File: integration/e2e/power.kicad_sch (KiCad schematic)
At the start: 2 parts

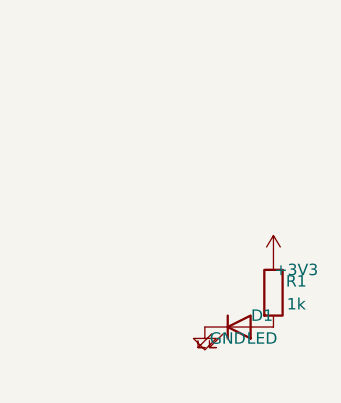
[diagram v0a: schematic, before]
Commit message: feat(e2e): lay out the e2e schematic with straight wires
The first e2e sheets connected parts pin to pin, on A4: correct (ERC
clean) but hard to read, with parts on top of each other in a corner.
Now:

* both sheets are A5, with title blocks (title, date, revision, a note);
* every wire is straight. On the root sheet, each pin of J1 runs left
  to its rail, +3V3 and its power flag above, GND and its flag below,
  with a junction on each rail. On "Power", +3V3, R1, D1 (turned so its
  anode is on top) and GND form one column;
* D1's reference and value read horizontally.

The nets, parts and UUIDs are unchanged, so the board still matches.
KiCad 9.0.9, on the design staged as kicad_pcb stages it: ERC 0
violations; DRC 0 violations, 0 unconnected, 0 parity issues; netlist
+3V3 (J1.1, R1.1), GND (D1.K, J1.2), Net-(D1-A) (D1.A, R1.2).

This commit has been created by an automated coding assistant,
with human supervision.

Prompt:
why do these sample e2e designs have doglegs in schematics, when all
wires could be mostly straight?

Co-Authored-By: Claude Opus 5.5 <noreply@anthropic.com>
Claude-Session: https://claude.ai/code/session_01WoWXzhMvNxH4iJRPTWT44f
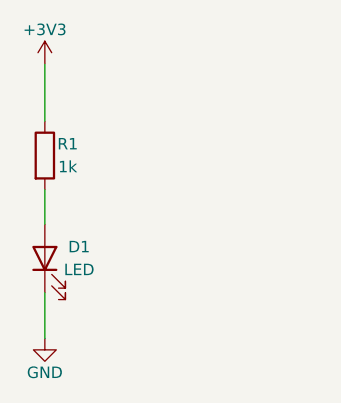
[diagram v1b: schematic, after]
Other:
- company: (none) -> rules_kicad
- title: (none) -> rules_kicad e2e design: Power
- moved on the sheet: D1, R1
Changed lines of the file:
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@@
 	(generator "eeschema")
 	(generator_version "9.0")
-	(paper "A4")
+	(paper "A5")
+	(title_block
+		(title "rules_kicad e2e design: Power")
+		(date "2026-10-29")
+		(rev "1")
+		(company "rules_kicad")
+		(comment 1 "R1 sets the LED current: (3.3 V - 2 V) / 1 kOhm = 1.3 mA")
+	)
+	(symbol
+		(lib_id "power:+3V3")
+		(at 76.2 50.8 0)
+		(unit 1)
+		(exclude_from_sim no)
+		(in_bom no)
+		(on_board no)
+		(dnp no)
+		(property "Reference" "#PWR03"
+			(at 76.2 44.45 0)
+			(effects
+				(font
+					(size 1.27 1.27)
+				)
+				(hide yes)
+			)
+		)
+		(property "Value" "+3V3"
+			(at 76.2 46.99 0)
+			(effects
+				(font
+					(size 1.27 1.27)
+				)
+			)
+		)
+		(property "Footprint" ""
+			(at 76.2 50.8 0)
+			(effects
+				(font
+					(size 1.27 1.27)
+				)
+				(hide yes)
+			)
+		)
+		(property "Datasheet" "~"
+			(at 76.2 50.8 0)
+			(effects
+				(font
+					(size 1.27 1.27)
+				)
+				(hide yes)
+			)
+		)
+		(property "Description" ""
+			(at 76.2 50.8 0)
+			(effects
+				(font
+					(size 1.27 1.27)
+				)
+				(hide yes)
+			)
+		)
+		(pin "1"
+		)
+		(instances
+			(project "main"
+				(path "/02c35194-34ab-516c-8342-afa9fed2f47f/4a82951d-9541-5098-92db-96b4b94b7393"
+					(reference "#PWR03")
+					(unit 1)
+				)
+			)
+		)
+	)
 	(symbol
 		(lib_id "Device:R")
-		(at 101.6 76.2 0)
+		(at 76.2 60.96 0)
 		(unit 1)
 		(exclude_from_sim no)
@@
 		(dnp no)
 		(property "Reference" "R1"
-			(at 104.14 74.93 0)
+			(at 78.74 59.69 0)
 			(effects
 				(font
@@
 		)
 		(property "Value" "1k"
-			(at 104.14 77.47 0)
+			(at 78.74 62.23 0)
 			(effects
 				(font
@@
 		)
 		(property "Footprint" "Resistor_SMD:R_0603_1608Metric"
-			(at 101.6 76.2 0)
-			(effects
-				(font
-					(size 1.27 1.27)
-				)
-				(hide yes)
-			)
-		)
-		(property "Datasheet" "~"
-			(at 101.6 76.2 0)
-			(effects
-				(font
-					(size 1.27 1.27)
-				)
-				(hide yes)
-			)
-		)
-		(property "Description" ""
-			(at 101.6 76.2 0)
+			(at 76.2 60.96 0)
+			(effects
+				(font
+					(size 1.27 1.27)
+				)
+				(hide yes)
+			)
+		)
+		(property "Datasheet" "~"
+			(at 76.2 60.96 0)
+			(effects
+				(font
+					(size 1.27 1.27)
+				)
+				(hide yes)
+			)
+		)
+		(property "Description" ""
+			(at 76.2 60.96 0)
 			(effects
 				(font
@@
 	(symbol
 		(lib_id "Device:LED")
-		(at 97.79 80.01 0)
+		(at 76.2 72.39 90)
 		(unit 1)
 		(exclude_from_sim no)
@@
 		(dnp no)
 		(property "Reference" "D1"
-			(at 100.33000000000001 78.74000000000001 0)
+			(at 80.01 71.12 90)
 			(effects
 				(font
@@
 		)
 		(property "Value" "LED"
-			(at 100.33000000000001 81.28 0)
+			(at 80.01 73.66 90)
 			(effects
 				(font
@@
 		)
 		(property "Footprint" "LED_SMD:LED_0603_1608Metric"
-			(at 97.79 80.01 0)
-			(effects
-				(font
-					(size 1.27 1.27)
-				)
-				(hide yes)
-			)
-		)
-		(property "Datasheet" "~"
-			(at 97.79 80.01 0)
-			(effects
-				(font
-					(size 1.27 1.27)
-				)
-				(hide yes)
-			)
-		)
-		(property "Description" ""
-			(at 97.79 80.01 0)
+			(at 76.2 72.39 0)
+			(effects
+				(font
+					(size 1.27 1.27)
+				)
+				(hide yes)
+			)
+		)
+		(property "Datasheet" "~"
+			(at 76.2 72.39 0)
+			(effects
+				(font
+					(size 1.27 1.27)
+				)
+				(hide yes)
+			)
+		)
+		(property "Description" ""
+			(at 76.2 72.39 0)
 			(effects
 				(font
@@
 	)
 	(symbol
-		(lib_id "power:+3V3")
-		(at 101.6 72.39 0)
+		(lib_id "power:GND")
+		(at 76.2 81.28 0)
 		(unit 1)
 		(exclude_from_sim no)
@@
 		(on_board no)
 		(dnp no)
-		(property "Reference" "#PWR03"
-			(at 104.14 71.12 0)
-			(effects
-				(font
-					(size 1.27 1.27)
-				)
-				(hide yes)
-			)
-		)
-		(property "Value" "+3V3"
-			(at 104.14 73.66 0)
+		(property "Reference" "#PWR04"
+			(at 76.2 87.63 0)
+			(effects
+				(font
+					(size 1.27 1.27)
+				)
+				(hide yes)
+			)
+		)
+		(property "Value" "GND"
+			(at 76.2 85.09 0)
 			(effects
 				(font
@@
 		)
 		(property "Footprint" ""
-			(at 101.6 72.39 0)
-			(effects
-				(font
-					(size 1.27 1.27)
-				)
-				(hide yes)
-			)
-		)
-		(property "Datasheet" "~"
-			(at 101.6 72.39 0)
-			(effects
-				(font
-					(size 1.27 1.27)
-				)
-				(hide yes)
-			)
-		)
-		(property "Description" ""
-			(at 101.6 72.39 0)
-			(effects
-				(font
-					(size 1.27 1.27)
-				)
-				(hide yes)
-			)
-		)
-		(pin "1"
-		)
-		(instances
-			(project "main"
-				(path "/02c35194-34ab-516c-8342-afa9fed2f47f/4a82951d-9541-5098-92db-96b4b94b7393"
-					(reference "#PWR03")
-					(unit 1)
-				)
-			)
-		)
-	)
-	(symbol
-		(lib_id "power:GND")
-		(at 93.98 80.01 0)
-		(unit 1)
-		(exclude_from_sim no)
-		(in_bom no)
-		(on_board no)
-		(dnp no)
-		(property "Reference" "#PWR04"
-			(at 96.52000000000001 78.74000000000001 0)
-			(effects
-				(font
-					(size 1.27 1.27)
-				)
-				(hide yes)
-			)
-		)
-		(property "Value" "GND"
-			(at 96.52000000000001 81.28 0)
-			(effects
-				(font
-					(size 1.27 1.27)
-				)
-			)
-		)
-		(property "Footprint" ""
-			(at 93.98 80.01 0)
-			(effects
-				(font
-					(size 1.27 1.27)
-				)
-				(hide yes)
-			)
-		)
-		(property "Datasheet" "~"
-			(at 93.98 80.01 0)
-			(effects
-				(font
-					(size 1.27 1.27)
-				)
-				(hide yes)
-			)
-		)
-		(property "Description" ""
-			(at 93.98 80.01 0)
+			(at 76.2 81.28 0)
+			(effects
+				(font
+					(size 1.27 1.27)
+				)
+				(hide yes)
+			)
+		)
+		(property "Datasheet" "~"
+			(at 76.2 81.28 0)
+			(effects
+				(font
+					(size 1.27 1.27)
+				)
+				(hide yes)
+			)
+		)
+		(property "Description" ""
+			(at 76.2 81.28 0)
 			(effects
 				(font
@@
 		)
 	)
+	(wire
+		(pts
+			(xy 76.2 50.8) (xy 76.2 57.15)
+		)
+		(stroke
+			(width 0)
+			(type default)
+		)
+	)
+	(wire
+		(pts
+			(xy 76.2 64.77) (xy 76.2 68.58)
+		)
+		(stroke
+			(width 0)
+			(type default)
+		)
+	)
+	(wire
+		(pts
+			(xy 76.2 76.2) (xy 76.2 81.28)
+		)
+		(stroke
+			(width 0)
+			(type default)
+		)
+	)
